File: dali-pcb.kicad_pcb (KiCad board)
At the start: 2 copper layers, 180.4 x 113 mm, 60 parts, among them J1 12-22.5V DC, J10 5V DC, J11 5V DC, J12 5V DC, J13 5V DC, J14 5V DC, J15 GND, J2 DALI BUS, J20 LOLIN-S3 (L), J21 LOLIN-S3 (R), J22 ESP32-S3-DEVKITC-1 (L), J23 ESP32-S3-DEVKITC-1 (R), J24 LOLIN-S3-MINI (L), J25 LOLIN-S3-MINI (R), J26 LOLIN-S2-MINI (L), J27 LOLIN-S2-MINI (R), J3 DALI BUS, J30 FTDI-MCU, J31 UART-DALI, J4 DALI BUS, J40 A10, J41 A5-1, J42 A5-2, J43 A2-1, J44 A2-2, J45 A2-3, J46 A2-4, J47 A2-5, J50 D8, J51 D4-1, J52 D4-2, J53 D2-1, J54 D2-2, J55 D2-3, J56 D2-4, J60 D1-11, J61 D1-12, J62 D1-13, J63 D1-14, Q1 PZT2222A, Q2 MMBT2222A, U1 TCLT1000, U2 TCLT1000

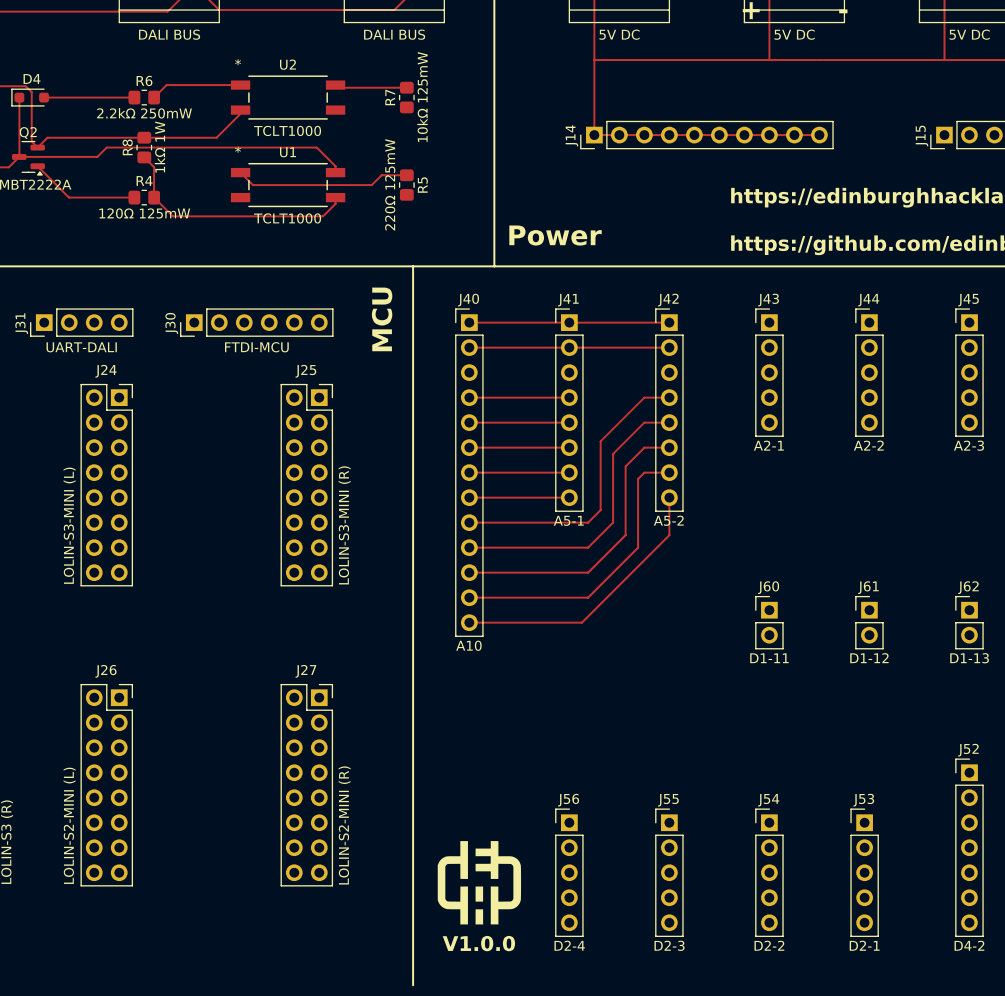
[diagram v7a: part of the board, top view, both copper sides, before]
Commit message: Move LOLIN mini boards further away from FTDI/UART pin headers
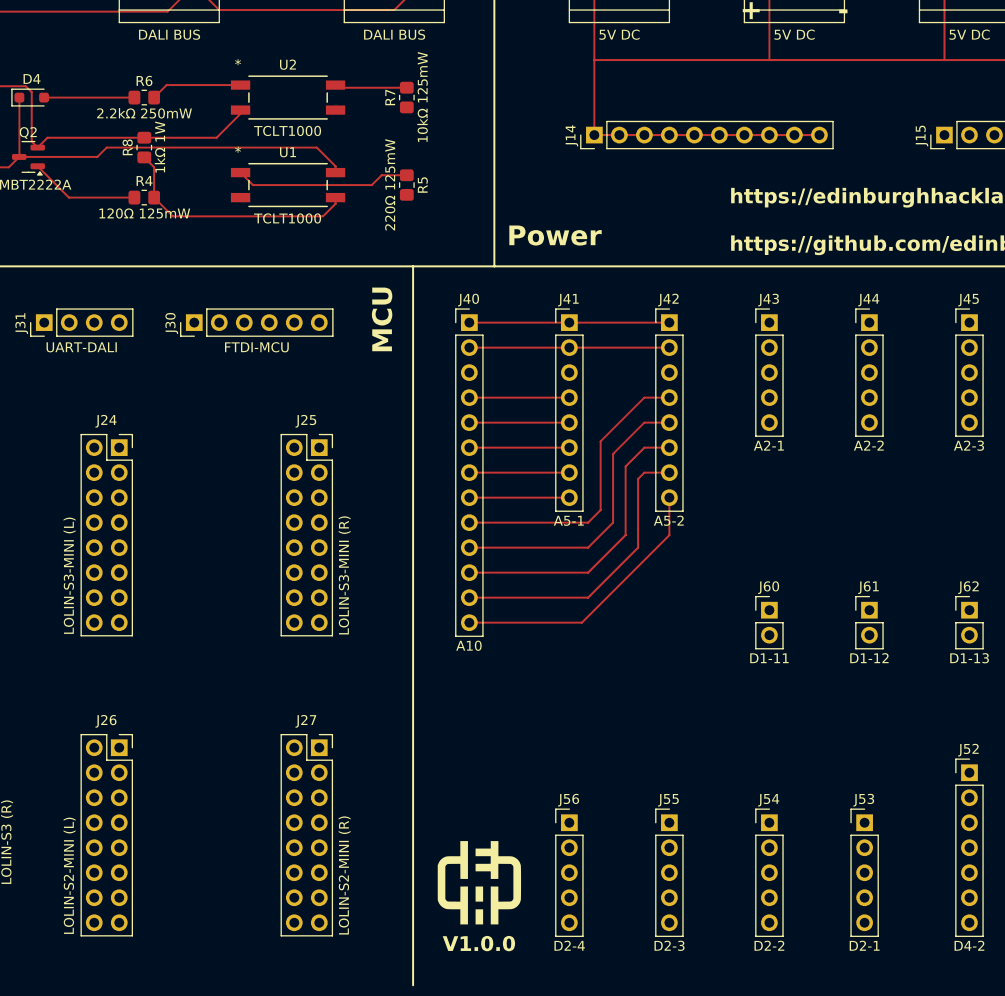
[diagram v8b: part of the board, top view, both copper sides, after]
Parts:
- moved J24 5.08 mm to (76.2, 68.6)
- moved J25 5.08 mm to (96.5, 68.6)
- moved J26 5.08 mm to (76.2, 99.1)
- moved J27 5.08 mm to (96.5, 99.1)
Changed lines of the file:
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@@
 	(footprint "Connector_PinSocket_2.54mm:PinSocket_2x08_P2.54mm_Vertical"
 		(layer "F.Cu")
-		(at 96.52 93.98)
+		(at 96.52 99.06)
 		(descr "Through hole straight socket strip, 2x08, 2.54mm pitch, double cols (from Kicad 4.0.7), script generated")
 		(tags "Through hole socket strip THT 2x08 2.54mm double row")
@@
 	(footprint "Connector_PinSocket_2.54mm:PinSocket_2x08_P2.54mm_Vertical"
 		(layer "F.Cu")
-		(at 96.52 63.5)
+		(at 96.52 68.58)
 		(descr "Through hole straight socket strip, 2x08, 2.54mm pitch, double cols (from Kicad 4.0.7), script generated")
 		(tags "Through hole socket strip THT 2x08 2.54mm double row")
@@
 	(footprint "Connector_PinSocket_2.54mm:PinSocket_2x08_P2.54mm_Vertical"
 		(layer "F.Cu")
-		(at 76.2 63.5)
+		(at 76.2 68.58)
 		(descr "Through hole straight socket strip, 2x08, 2.54mm pitch, double cols (from Kicad 4.0.7), script generated")
 		(tags "Through hole socket strip THT 2x08 2.54mm double row")
@@
 	(footprint "Connector_PinSocket_2.54mm:PinSocket_2x08_P2.54mm_Vertical"
 		(layer "F.Cu")
-		(at 76.2 93.98)
+		(at 76.2 99.06)
 		(descr "Through hole straight socket strip, 2x08, 2.54mm pitch, double cols (from Kicad 4.0.7), script generated")
 		(tags "Through hole socket strip THT 2x08 2.54mm double row")
@@
 	)
 	(segment
-		(start 147.32 29.21)
+		(start 143.51 29.21)
 		(end 160.02 29.21)
 		(width 0.2)
@@
 		(width 0.2)
 		(layer "F.Cu")
-		(net 10)
-	)
-	(segment
-		(start 143.51 29.21)
-		(end 147.32 29.21)
-		(width 0.2)
-		(layer "F.Cu")
